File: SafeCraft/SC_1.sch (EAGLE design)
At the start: 19 parts, among them IC1 TS555, Q1 DSS20201L-7

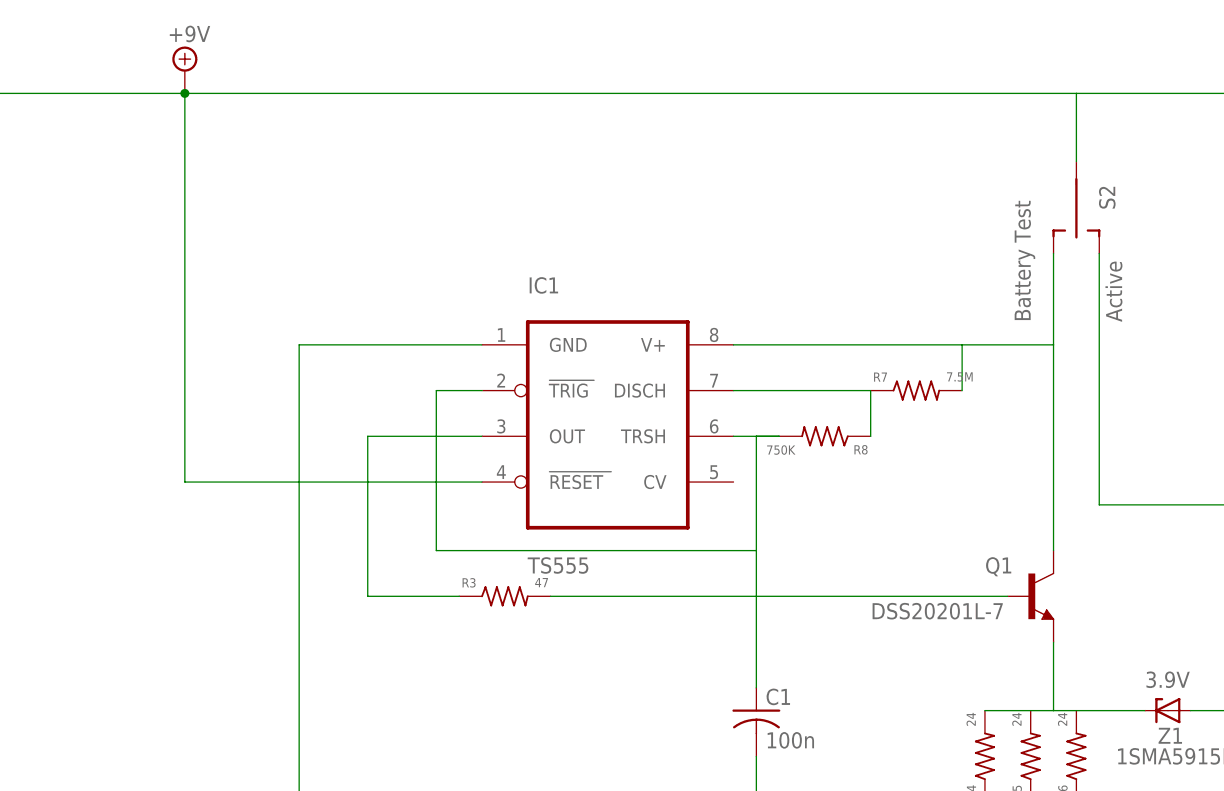
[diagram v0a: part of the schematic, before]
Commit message: updated schematic for reset line and PNP transistor
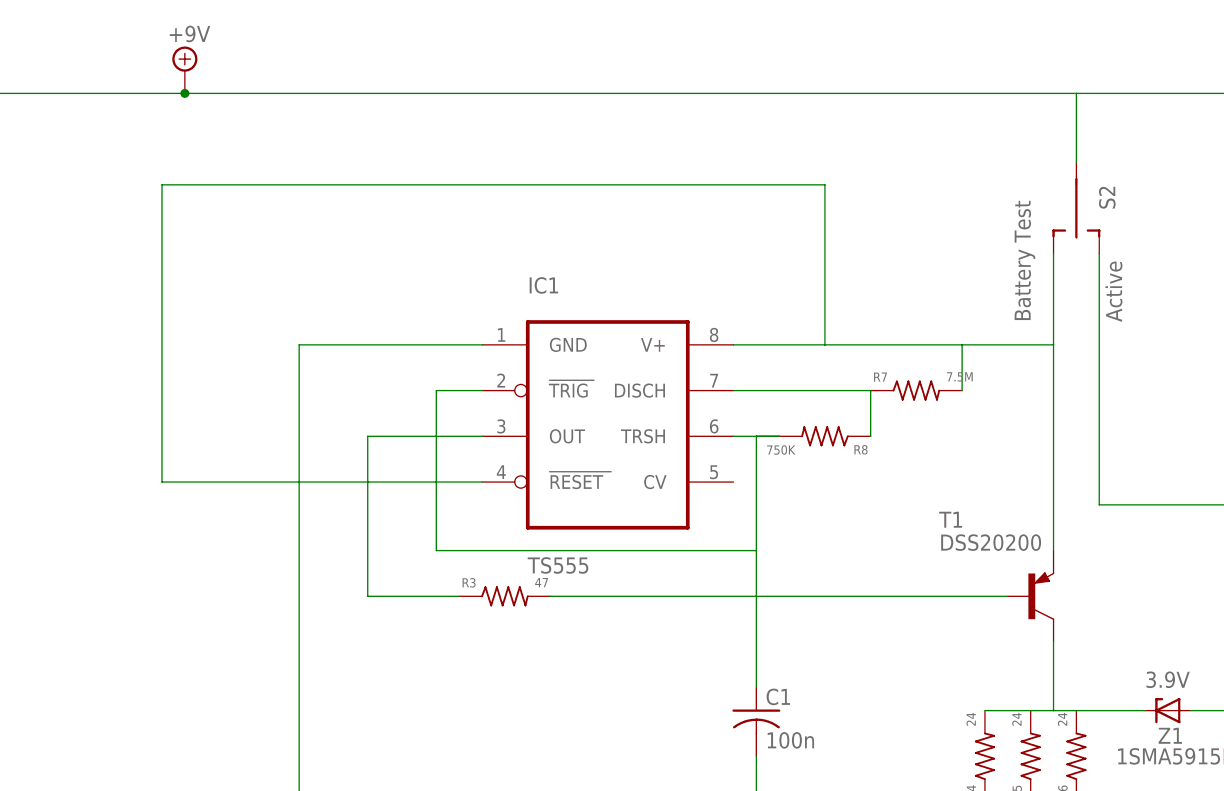
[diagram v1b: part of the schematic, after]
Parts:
- removed Q1: DSS20201L-7, transistor-npn:BC817-16SMD
- added T1: DSS20200, transistor:BC807-16-PNP-SOT23-BEC
- LED1, LED2: device led:LEDP-LCC-2-BACK -> led:LEDP-LCC-2
- Z1: device diode:ZENER-DIODESMA -> diode:ZENER-DIODESMB
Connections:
- removed net N$3: IC1.V+, Q1.C, R7.2, S2.S
- new net N$1: IC1.RESET, IC1.V+, R7.2, S2.S, T1.E
- net +9V: no longer IC1.RESET
- net N$13: now also T1.C; no longer Q1.E
- net N$9: now also T1.B; no longer Q1.B

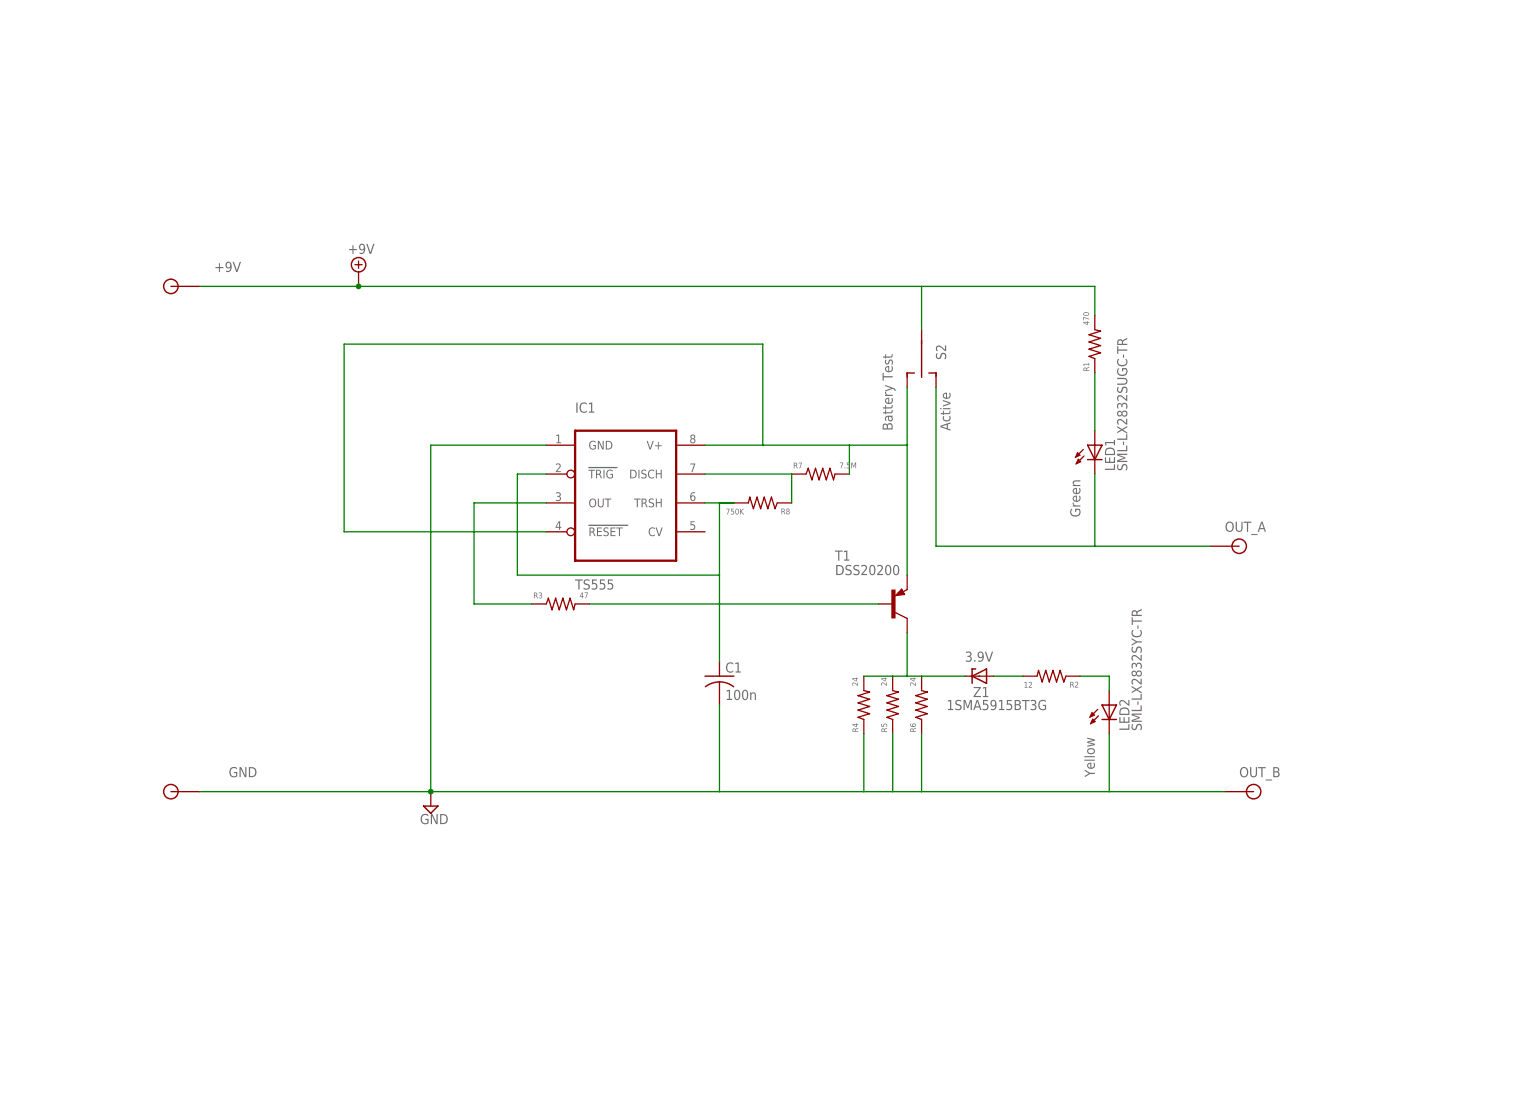
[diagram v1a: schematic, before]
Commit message: 
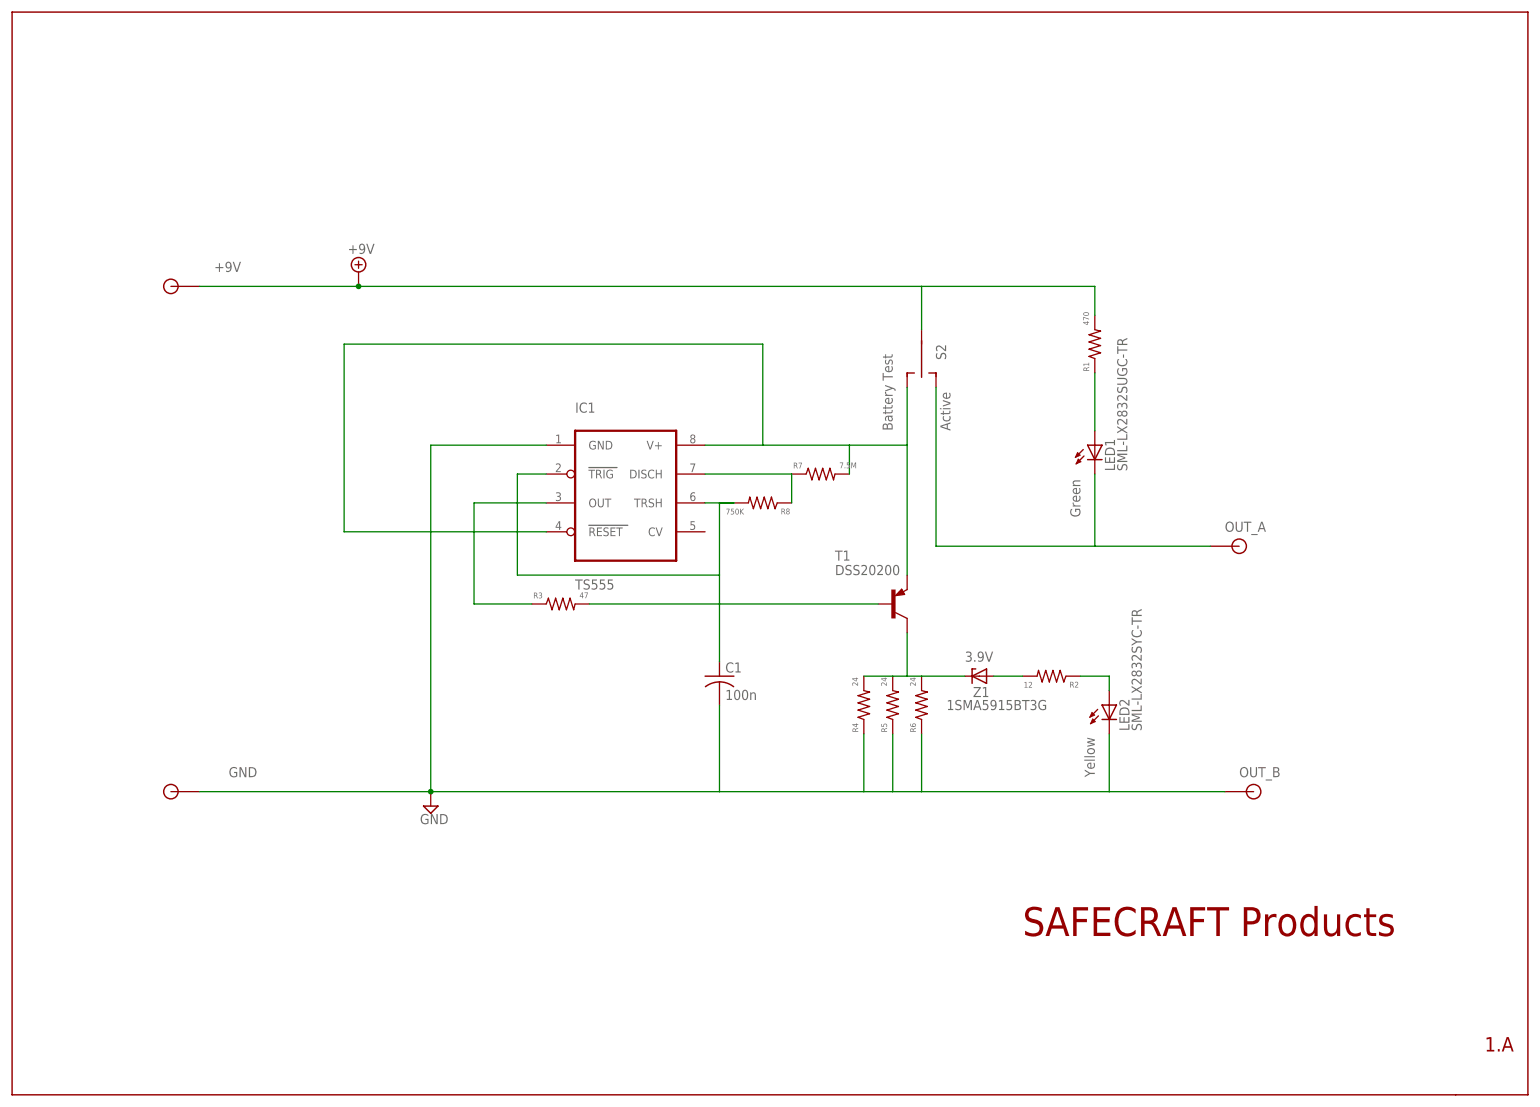
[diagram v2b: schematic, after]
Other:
- note added: "1.A"
- note added: "SAFECRAFT Products"
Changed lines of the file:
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@@
 <grid distance="0.1" unitdist="inch" unit="inch" style="lines" multiple="1" display="no" altdistance="0.01" altunitdist="inch" altunit="inch"/>
 <layers>
-<layer number="1" name="Top" color="4" fill="1" visible="yes" active="no"/>
-<layer number="2" name="Route2" color="1" fill="3" visible="yes" active="no"/>
-<layer number="3" name="Route3" color="4" fill="3" visible="yes" active="no"/>
-<layer number="4" name="Route4" color="1" fill="4" visible="yes" active="no"/>
-<layer number="5" name="Route5" color="4" fill="4" visible="yes" active="no"/>
-<layer number="6" name="Route6" color="1" fill="8" visible="yes" active="no"/>
-<layer number="7" name="Route7" color="4" fill="8" visible="yes" active="no"/>
-<layer number="8" name="Route8" color="1" fill="2" visible="yes" active="no"/>
-<layer number="9" name="Route9" color="4" fill="2" visible="yes" active="no"/>
-<layer number="10" name="Route10" color="1" fill="7" visible="yes" active="no"/>
-<layer number="11" name="Route11" color="4" fill="7" visible="yes" active="no"/>
-<layer number="12" name="Route12" color="1" fill="5" visible="yes" active="no"/>
-<layer number="13" name="Route13" color="4" fill="5" visible="yes" active="no"/>
-<layer number="14" name="Route14" color="1" fill="6" visible="yes" active="no"/>
-<layer number="15" name="Route15" color="4" fill="6" visible="yes" active="no"/>
-<layer number="16" name="Bottom" color="1" fill="1" visible="yes" active="no"/>
-<layer number="17" name="Pads" color="2" fill="1" visible="yes" active="no"/>
-<layer number="18" name="Vias" color="2" fill="1" visible="yes" active="no"/>
-<layer number="19" name="Unrouted" color="6" fill="1" visible="yes" active="no"/>
-<layer number="20" name="Dimension" color="15" fill="1" visible="yes" active="no"/>
-<layer number="21" name="tPlace" color="7" fill="1" visible="yes" active="no"/>
-<layer number="22" name="bPlace" color="7" fill="1" visible="yes" active="no"/>
-<layer number="23" name="tOrigins" color="15" fill="1" visible="yes" active="no"/>
-<layer number="24" name="bOrigins" color="15" fill="1" visible="yes" active="no"/>
-<layer number="25" name="tNames" color="7" fill="1" visible="yes" active="no"/>
-<layer number="26" name="bNames" color="7" fill="1" visible="yes" active="no"/>
-<layer number="27" name="tValues" color="7" fill="1" visible="yes" active="no"/>
-<layer number="28" name="bValues" color="7" fill="1" visible="yes" active="no"/>
+<layer number="1" name="Top" color="4" fill="1" visible="no" active="no"/>
+<layer number="2" name="Route2" color="1" fill="3" visible="no" active="no"/>
+<layer number="3" name="Route3" color="4" fill="3" visible="no" active="no"/>
+<layer number="4" name="Route4" color="1" fill="4" visible="no" active="no"/>
+<layer number="5" name="Route5" color="4" fill="4" visible="no" active="no"/>
+<layer number="6" name="Route6" color="1" fill="8" visible="no" active="no"/>
+<layer number="7" name="Route7" color="4" fill="8" visible="no" active="no"/>
+<layer number="8" name="Route8" color="1" fill="2" visible="no" active="no"/>
+<layer number="9" name="Route9" color="4" fill="2" visible="no" active="no"/>
+<layer number="10" name="Route10" color="1" fill="7" visible="no" active="no"/>
+<layer number="11" name="Route11" color="4" fill="7" visible="no" active="no"/>
+<layer number="12" name="Route12" color="1" fill="5" visible="no" active="no"/>
+<layer number="13" name="Route13" color="4" fill="5" visible="no" active="no"/>
+<layer number="14" name="Route14" color="1" fill="6" visible="no" active="no"/>
+<layer number="15" name="Route15" color="4" fill="6" visible="no" active="no"/>
+<layer number="16" name="Bottom" color="1" fill="1" visible="no" active="no"/>
+<layer number="17" name="Pads" color="2" fill="1" visible="no" active="no"/>
+<layer number="18" name="Vias" color="2" fill="1" visible="no" active="no"/>
+<layer number="19" name="Unrouted" color="6" fill="1" visible="no" active="no"/>
+<layer number="20" name="Dimension" color="15" fill="1" visible="no" active="no"/>
+<layer number="21" name="tPlace" color="7" fill="1" visible="no" active="no"/>
+<layer number="22" name="bPlace" color="7" fill="1" visible="no" active="no"/>
+<layer number="23" name="tOrigins" color="15" fill="1" visible="no" active="no"/>
+<layer number="24" name="bOrigins" color="15" fill="1" visible="no" active="no"/>
+<layer number="25" name="tNames" color="7" fill="1" visible="no" active="no"/>
+<layer number="26" name="bNames" color="7" fill="1" visible="no" active="no"/>
+<layer number="27" name="tValues" color="7" fill="1" visible="no" active="no"/>
+<layer number="28" name="bValues" color="7" fill="1" visible="no" active="no"/>
 <layer number="29" name="tStop" color="7" fill="3" visible="no" active="no"/>
 <layer number="30" name="bStop" color="7" fill="6" visible="no" active="no"/>
@@
 <layer number="35" name="tGlue" color="7" fill="4" visible="no" active="no"/>
 <layer number="36" name="bGlue" color="7" fill="5" visible="no" active="no"/>
-<layer number="37" name="tTest" color="7" fill="1" visible="yes" active="no"/>
-<layer number="38" name="bTest" color="7" fill="1" visible="yes" active="no"/>
+<layer number="37" name="tTest" color="7" fill="1" visible="no" active="no"/>
+<layer number="38" name="bTest" color="7" fill="1" visible="no" active="no"/>
 <layer number="39" name="tKeepout" color="4" fill="11" visible="no" active="no"/>
 <layer number="40" name="bKeepout" color="1" fill="11" visible="no" active="no"/>
@@
 <layer number="44" name="Drills" color="7" fill="1" visible="no" active="no"/>
 <layer number="45" name="Holes" color="7" fill="1" visible="no" active="no"/>
-<layer number="46" name="Milling" color="3" fill="1" visible="yes" active="no"/>
-<layer number="47" name="Measures" color="7" fill="1" visible="yes" active="no"/>
-<layer number="48" name="Document" color="7" fill="1" visible="yes" active="no"/>
-<layer number="49" name="Reference" color="7" fill="1" visible="yes" active="no"/>
-<layer number="50" name="dxf" color="7" fill="1" visible="yes" active="no"/>
-<layer number="51" name="tDocu" color="7" fill="1" visible="yes" active="no"/>
-<layer number="52" name="bDocu" color="7" fill="1" visible="yes" active="no"/>
-<layer number="53" name="tPadExt" color="7" fill="1" visible="yes" active="no"/>
-<layer number="54" name="bPadExt" color="1" fill="1" visible="yes" active="no"/>
+<layer number="46" name="Milling" color="3" fill="1" visible="no" active="no"/>
+<layer number="47" name="Measures" color="7" fill="1" visible="no" active="no"/>
+<layer number="48" name="Document" color="7" fill="1" visible="no" active="no"/>
+<layer number="49" name="Reference" color="7" fill="1" visible="no" active="no"/>
+<layer number="50" name="dxf" color="7" fill="1" visible="no" active="no"/>
+<layer number="51" name="tDocu" color="7" fill="1" visible="no" active="no"/>
+<layer number="52" name="bDocu" color="7" fill="1" visible="no" active="no"/>
+<layer number="53" name="tPadExt" color="7" fill="1" visible="no" active="no"/>
+<layer number="54" name="bPadExt" color="1" fill="1" visible="no" active="no"/>
 <layer number="91" name="Nets" color="2" fill="1" visible="yes" active="yes"/>
 <layer number="92" name="Busses" color="1" fill="1" visible="yes" active="yes"/>
@@
 <part name="U$4" library="1AA_Stofer" deviceset="SOLDERPAD_NOHOLE" device=""/>
 <part name="T1" library="transistor" deviceset="*-PNP-" device="SOT23-BEC" technology="BC807-16" value="DSS20200"/>
+<part name="U$5" library="1AA_Stofer" deviceset="8.5X11" device=""/>
 </parts>
 <sheets>
@@
 <text x="160.02" y="10.16" size="1.778" layer="96">OUT_B</text>
 <text x="111.76" y="30.48" size="1.778" layer="96">3.9V</text>
+<text x="203.2" y="-38.1" size="2.54" layer="94">1.A</text>
+<text x="121.92" y="-17.78" size="5.08" layer="94">SAFECRAFT Products</text>
 </plain>
 <instances>
@@
 <instance part="U$4" gate="G$1" x="-27.94" y="7.62"/>
 <instance part="T1" gate="G$1" x="99.06" y="40.64"/>
+<instance part="U$5" gate="G$1" x="-55.88" y="-45.72"/>
+<instance part="U$5" gate="G$2" x="109.22" y="-45.72"/>
 </instances>
 <busses>

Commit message: 
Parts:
- T1: value DSS20200 -> FMMT718TA
- Z1: value 1SMA5915BT3G -> 1SMA5917BT3G
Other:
- note added: "4.7V"
- note removed: "3.9V"
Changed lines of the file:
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@@
 <part name="LED2" library="led" deviceset="LED" device="P-LCC-2" value="SML-LX2832SYC-TR"/>
 <part name="R2" library="rcl" deviceset="R-US_" device="R0805" value="12"/>
-<part name="Z1" library="diode" deviceset="ZENER-DIODE" device="SMB" value="1SMA5915BT3G"/>
+<part name="Z1" library="diode" deviceset="ZENER-DIODE" device="SMB" value="1SMA5917BT3G"/>
 <part name="R8" library="rcl" deviceset="R-US_" device="R0805" value="750K"/>
 <part name="R7" library="rcl" deviceset="R-US_" device="R0805" value="7.5M"/>
@@
 <part name="U$3" library="1AA_Stofer" deviceset="SOLDERPAD_NOHOLE" device=""/>
 <part name="U$4" library="1AA_Stofer" deviceset="SOLDERPAD_NOHOLE" device=""/>
-<part name="T1" library="transistor" deviceset="*-PNP-" device="SOT23-BEC" technology="BC807-16" value="DSS20200"/>
+<part name="T1" library="transistor" deviceset="*-PNP-" device="SOT23-BEC" technology="BC807-16" value="FMMT718TA"/>
 <part name="U$5" library="1AA_Stofer" deviceset="8.5X11" device=""/>
 </parts>
@@
 <text x="99.06" y="71.12" size="1.778" layer="96" rot="R90">Battery Test</text>
 <text x="160.02" y="10.16" size="1.778" layer="96">OUT_B</text>
-<text x="111.76" y="30.48" size="1.778" layer="96">3.9V</text>
 <text x="203.2" y="-38.1" size="2.54" layer="94">1.A</text>
 <text x="121.92" y="-17.78" size="5.08" layer="94">SAFECRAFT Products</text>
+<text x="111.76" y="30.48" size="1.778" layer="96">4.7V</text>
 </plain>
 <instances>
